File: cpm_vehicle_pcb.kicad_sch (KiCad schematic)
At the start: 77 parts, among them IC1 ATMEGAAU, IC2 RPI-ZERO, J1 Conn_02x03_Counter_Clockwise, J2 Conn_02x03_Counter_Clockwise, J3 Conn_01x05, J4 AVR-ISP-6, P1 NCP1117, P2 OSTTE020104, Q01 IRF3808, Q11 BSS123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

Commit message: BMS
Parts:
- added C8, C9: 100nF, footprints_vehicle_pcb:C0805_10681391, symbol main_board_V2.4-eagle-import:embedded_10681391_C-EUC0805
- added Q2, Q3: DMG9926UDM, Package_TO_SOT_SMD:SOT-23-6, symbol Transistor_FET:DMG9926UDM
- added R22, R24: 330, symbol Device:R
- added R23, R25: 2.7K, symbol Device:R
- added U5, U6: AP9101CK6, Package_TO_SOT_SMD:SOT-23-6, symbol Battery_Management:AP9101CK6
- C3: value 100nF -> 10uF
- C4, C7: value 100nF -> 22uF
- C5: value 100nF -> 10nuF
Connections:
- net GND: now also C3.2, C4.2, C5.2, C6.1, C7.1, MCP1.6 (VSS), R21.2, U4.2 (GND), C9.1, Q3.3 (S2), U6.6 (VSS)
- net +7.5V: now reaches C5.1, MCP1.7 (VBAT), SI1. (D)
- net +7.5V: now also R22.1
- new net: Q3.4 (G2), U6.1 (DO)
- new net: R25.1, U6.2 (VM)
- new net: Q3.6 (G1), U6.3 (CO)
- new net: C9.2, R24.2, U6.5 (VDD)
- new net: Q3.2 (S1/D2), Q3.5 (S1/D2)
- new net: Q2.2 (S1/D2), Q2.5 (S1/D2)
- new net: Q2.4 (G2), U5.1 (DO)
- new net: Q2.6 (G1), U5.3 (CO)
- new net: R23.1, U5.2 (VM)
- new net: C8.2, R22.2, U5.5 (VDD)
- new net +3.3V: C8.1, Q2.1 (D1), Q2.3 (S2), R23.2, R24.1, U5.6 (VSS)
- new net P-: Q3.1 (D1), R25.2
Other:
- note added: "Battery"
- note added: "Charger"

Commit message: usb to serial and some external pin and led circuit changes
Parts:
- added C10: 10nF, footprints_vehicle_pcb:C0805_10681391, symbol main_board_V2.4-eagle-import:embedded_10681391_C-EUC0805
- added J5: USB_B_Mini, symbol Connector:USB_B_Mini
- added QG2: XO91, footprints_vehicle_pcb:SM77H_crystal_oscillator, symbol main_board_V2.4-eagle-import:embedded_10681391_XO91
- added R26, R27: 1k, symbol Device:R
- added SW1: SW_DIP_x02, symbol Switch:SW_DIP_x02
- added U7: CH340G, Package_SO:SOIC-16_3.9x9.9mm_P1.27mm, symbol Interface_USB:CH340G
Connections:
- net +3V3: now also SW1.4; no longer C41.1, U3.1 (VCCA)
- net +5V: now also D2.2 (A), C10.2, J5.1 (VBUS), QG2.1 (E/D), QG2.4 (VCC), SW1.3, U7.16 (VCC); no longer C42.1, D2.1 (K), R10.2, U3.14 (VCCB)
- net ERW5: now also IC1.15 (PH3(OC4A)); no longer IC1.75 ((AD3)PA3)
- net ERW6: now also IC1.16 (PH4(OC4B)); no longer IC1.76 ((AD2)PA2)
- net ERW7: now also IC1.24 ((OC1A/PCINT5)PB5); no longer IC1.77 ((AD1)PA1)
- net ERW8: now also IC1.23 ((OC2A/PCINT4)PB4); no longer IC1.78 ((AD0)PA0)
- net GND: now also C10.1, J5.5 (GND), J5.6 (Shield), QG2.2 (GND), U7.1 (GND)
- net LED_BUILT_IN: now also IC1.25 ((OC1B/PCINT6)PB6), R10.2; no longer D3.2 (A), IC1.54 ((A9)PC1), R10.1
- net at R9.1: now also D2.1 (K); no longer D2.2 (A)
- net TX0: now reaches IC1.3 ((TXD0)PE1)
- net TX0: now also R27.2
- net RX0: now reaches IC1.4 ((XCK0/AIN0)PE2)
- net RX0: now also R26.2
- new net: D3.2 (A), R10.1
- new net: J5.2 (D-), U7.6 (UD-)
- new net: J5.3 (D+), U7.5 (UD+)
- new net: C42.1, SW1.2, U3.14 (VCCB)
- new net: C41.1, SW1.1, U3.1 (VCCA)
- new net: R27.1, U7.2 (TXD)
- new net: R26.1, U7.3 (RXD)
- new net: QG2.3 (OUT), U7.7 (XI)
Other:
- moved on the sheet: C71, D2, QG1, R10

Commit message: Small footprint changes
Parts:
- removed C01: 10uF, footprints_vehicle_pcb:UD-4X5,8_Electrolytic_cap, symbol main_board_V2.4-eagle-import:embedded_10681391_CPOL/4X5,8
- removed C02, C6, C8: 100nF, footprints_vehicle_pcb:C0805_10681391, symbol main_board_V2.4-eagle-import:embedded_10681391_C-EUC0805
- removed C5: 10nuF, footprints_vehicle_pcb:C0805_10681391, symbol main_board_V2.4-eagle-import:embedded_10681391_C-EUC0805
- removed D01: BAS40-04, footprints_vehicle_pcb:SOT23_BAS40_04_schottky_diode, symbol main_board_V2.4-eagle-import:embedded_10681391_BAS40-04
- removed D6: LED, symbol Device:LED
- removed MCP1: ~, symbol MCP73844:MCP73844
- removed Q01: IRF3808, footprints_vehicle_pcb:TO220_IRF3808PBF, symbol main_board_V2.4-eagle-import:embedded_10681391_IRF3808
- removed Q2: DMG9926UDM, Package_TO_SOT_SMD:SOT-23-6, symbol Transistor_FET:DMG9926UDM
- removed R03: 1.5k, footprints_vehicle_pcb:R0805_10681391, symbol main_board_V2.4-eagle-import:embedded_10681391_R-EUR0805
- removed R04: 12k, footprints_vehicle_pcb:R0805_10681391, symbol main_board_V2.4-eagle-import:embedded_10681391_R-EUR0805
- removed R05, R06: 0, footprints_vehicle_pcb:R0805_10681391, symbol main_board_V2.4-eagle-import:embedded_10681391_R-EUR0805
- removed R07, R08: 560k, footprints_vehicle_pcb:R0805_10681391, symbol main_board_V2.4-eagle-import:embedded_10681391_R-EUR0805
- removed R19: 100mΩ, PCM_JLCPCB:R_1206, symbol PCM_JLCPCB-Resistors:1206,100mΩ
- removed R20: R, symbol Device:R
- removed R22: 330, symbol Device:R
- removed R23: 2.7K, symbol Device:R
- removed Rk1, Rk2: 24k, footprints_vehicle_pcb:R0805_10681391, symbol main_board_V2.4-eagle-import:embedded_10681391_R-EUR0805
- removed SI1: ~, symbol SI9433:SI9433_MOSFET
- removed U1: LM385-1.2/NOPB, footprints_vehicle_pcb:SO08_LM385, symbol main_board_V2.4-eagle-import:embedded_10681391_LM385-1.2/NOPB
- removed U2: LM358D, footprints_vehicle_pcb:SO08_comparator, symbol main_board_V2.4-eagle-import:embedded_10681391_LM358D
- removed U5, U6: AP9101CK6, Package_TO_SOT_SMD:SOT-23-6, symbol Battery_Management:AP9101CK6
- added C11: 100nF, footprints_vehicle_pcb:C0805_10681391, symbol main_board_V2.4-eagle-import:embedded_10681391_C-EUC0805
- added R28: 330, Resistor_SMD:R_0603_1608Metric, symbol Device:R
- added SW2: SW_SPDT_312, Button_Switch_THT:SW_Slide-03_Wuerth-WS-SLTV_10x2.5x6.4_P2.54mm, symbol Switch:SW_SPDT_312
- added U8: R5460N, PCM_JLCPCB:SOT-23-6_L2.9-W1.6-P0.95-LS2.8-BL, symbol PCM_JLCPCB-Power:Battery, Li-Ion, 0.5A, TP4057
- C31: footprint footprints_vehicle_pcb:UD-6,3X5,8_Electrolytic_CAP -> Capacitor_SMD:C_1206_3216Metric
- C4, C7: value 22uF -> 220uF
- J5: footprint (none) -> Connector_USB:USB_Mini-B_AdamTech_MUSB-B5-S-VT-TSMT-1_SMD_Vertical
- R1, R10, R11, R12, R13, R14, R15, R16, R17, R18, R2, R3o1, R9: footprint footprints_vehicle_pcb:R0805_10681391 -> Resistor_SMD:R_0603_1608Metric
- R24: value 330 -> 1K; footprint (none) -> Resistor_SMD:R_0603_1608Metric
- R25: value 2.7K -> 330; footprint (none) -> Resistor_SMD:R_0603_1608Metric
- R26, R27: footprint (none) -> Resistor_SMD:R_0603_1608Metric
- RV1: footprint (none) -> Potentiometer_SMD:Potentiometer_Bourns_3214W_Vertical
- SW1: footprint (none) -> Button_Switch_SMD:SW_DIP_SPSTx02_Slide_9.78x7.26mm_W8.61mm_P2.54mm
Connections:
- net BAT_GND is gone; now on net GND_battery: C81.-, P2.2
- net +7.5V: now also C3.1, D5.1 (K), SW2.2 (C)
- net GND: now also Q3.1 (D1), R24.2; no longer C3.2, C4.2, C7.1, C9.1, Q3.3 (S2), R21.2, U4.2 (GND)
- net VCC_BAT: no longer C61.1, C81.+, J3.2 (Pin_2), P1.3 (VIN), P2.1
- net at Q3.4 (G2): now also U8.1 (DOUT)
- net vcc_bat: now reaches R25.1
- net vcc_bat: now also C61.1, C81.+, J3.2 (Pin_2), P1.3 (VIN), P2.1, SW2.3 (A)
- net at Q3.6 (G1): now also U8.2 (COUT)
- net GND_battery: now reaches C9.2
- net GND_battery: now also C3.2, C4.2, C7.1, Q3.3 (S2), R21.2, U4.2 (GND), C11.2, U8.6 (VSS); no longer R24.2
- net +3.3V: no longer names the net of R24.1
- net +3.3V: now also U8.3 (V-)
- net P-: no longer names the net of R25.2
- net P-: now also C11.1, U8.5 (VDD); no longer Q3.1 (D1)
- new net: C9.1, R28.2, U8.4 (VC)
- new net BB: R28.1
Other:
- note removed: "Battery"
- moved on the sheet: C10, C3, C4, C61, C62, C63, C7, C71, D2, D3, D4, D5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

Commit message: update
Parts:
- C31: footprint Capacitor_SMD:C_1206_3216Metric -> Capacitor_THT:CP_Radial_D6.3mm_P2.50mm
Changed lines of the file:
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@@
 			)
 		)
-		(property "Footprint" "Capacitor_SMD:C_1206_3216Metric"
+		(property "Footprint" "Capacitor_THT:CP_Radial_D6.3mm_P2.50mm"
 			(at 414.02 76.2 0)
 			(effects

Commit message: Net class defined
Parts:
- C4, C7: value 220uF -> 22uF
- L1: value L -> 20uH
- R21: value R -> 3.3K; footprint (none) -> Resistor_SMD:R_0603_1608Metric
- R51, R52: footprint footprints_vehicle_pcb:R0805_10681391 -> Resistor_SMD:R_0603_1608Metric
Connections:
- net VCC_BAT is gone; now on net vcc_bat: R51.2
- net +7.5V: now also C81.+, P2.1
- net SERVO_PWM: now also IC1.7 ((OC3C/INT5)PE5)
- net vcc_bat: no longer C81.+, P2.1
- net TCK: no longer names the net of IC1.93 ((ADC4/TCK)PF4)
- net TDI: no longer names the net of IC1.90 ((ADC7/TDI)PF7)
- net TDO: no longer names the net of IC1.91 ((ADC6/TDO)PF6)
- net TMS: no longer names the net of IC1.92 ((ADC5/TMS)PF5)
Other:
- moved on the sheet: R24

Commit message: some minute changes
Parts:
- removed C31: 220uF, Capacitor_THT:CP_Radial_D6.3mm_P2.50mm, symbol main_board_V2.4-eagle-import:embedded_10681391_CPOL/6,3X7,7
- removed C63, C81: 220uF, footprints_vehicle_pcb:UD-6,3X5,8_Electrolytic_CAP, symbol main_board_V2.4-eagle-import:embedded_10681391_CPOL/6,3X7,7
- removed D4, D5: D_Schottky, symbol Device:D_Schottky
- removed J4: AVR-ISP-6, footprints_vehicle_pcb:AVR_ISP_6_footprint, symbol Connector:AVR-ISP-6
- removed P2: OSTTE020104, TerminalBlock:TerminalBlock_MaiXu_MX126-5.0-02P_1x02_P5.00mm, symbol pole_screw_term_2:OSTTE020104
- added C31, C63: 220uF, footprints_vehicle_pcb:C0805_10681391, symbol main_board_V2.4-eagle-import:embedded_10681391_C-EUC0805
- added D1, D6: SS54, PCM_JLCPCB:D_SMA, symbol PCM_JLCPCB-Diodes:Schottky,SS54
- added J6: Conn_01x03_Socket, Connector_PinSocket_2.54mm:PinSocket_1x03_P2.54mm_Horizontal, symbol Connector:Conn_01x03_Socket
- C4, C7: footprint footprints_vehicle_pcb:C0805_10681391 -> Capacitor_SMD:C_0603_1608Metric
- J2: footprint footprints_vehicle_pcb:JST_B5B-XH-A -> footprints_vehicle_pcb:HARWIN_M20-9980346
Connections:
- net +5V: now also C31.1, C63.1
- net BB: now also J6.2 (Pin_2)
- net GND: now also C3.2, C4.2, C7.1, R21.2, U4.2 (GND), C31.2, C63.2
- net vcc_bat: now also SW2.2 (C); no longer R25.1, SW2.3 (A)
- net at C4.1, RV1.1: now also D1.1, D6.2
- net at L1.2, U4.1 (SW): now also D1.2
- net B+: now reaches SW2.1 (B)
- net B+: now also R25.1, J6.3 (Pin_3)
- net +7.5V renamed +8.5V
- net +8.5V: now also SW2.3 (A), D6.1; no longer SW2.2 (C)
- removed net GND_battery: C11.2, C3.2, C4.2, C7.1, C9.2, Q3.3 (S2), R21.2, U4.2 (GND), U8.6 (VSS)
- new net B-: C11.2, C9.2, J6.1 (Pin_1), Q3.3 (S2), U8.6 (VSS)
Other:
- note removed: "(For Powering ESC)"
- moved on the sheet: SW2

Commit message: update
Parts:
- added R3, R4: 10k, Resistor_SMD:R_0603_1608Metric, symbol Device:R
- L1: footprint (none) -> Inductor_SMD:L_10.4x10.4_H4.8
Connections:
- net +5V: now also R3.2, R4.2
- net SCL: now also R4.1
- net SDA: now also R3.1

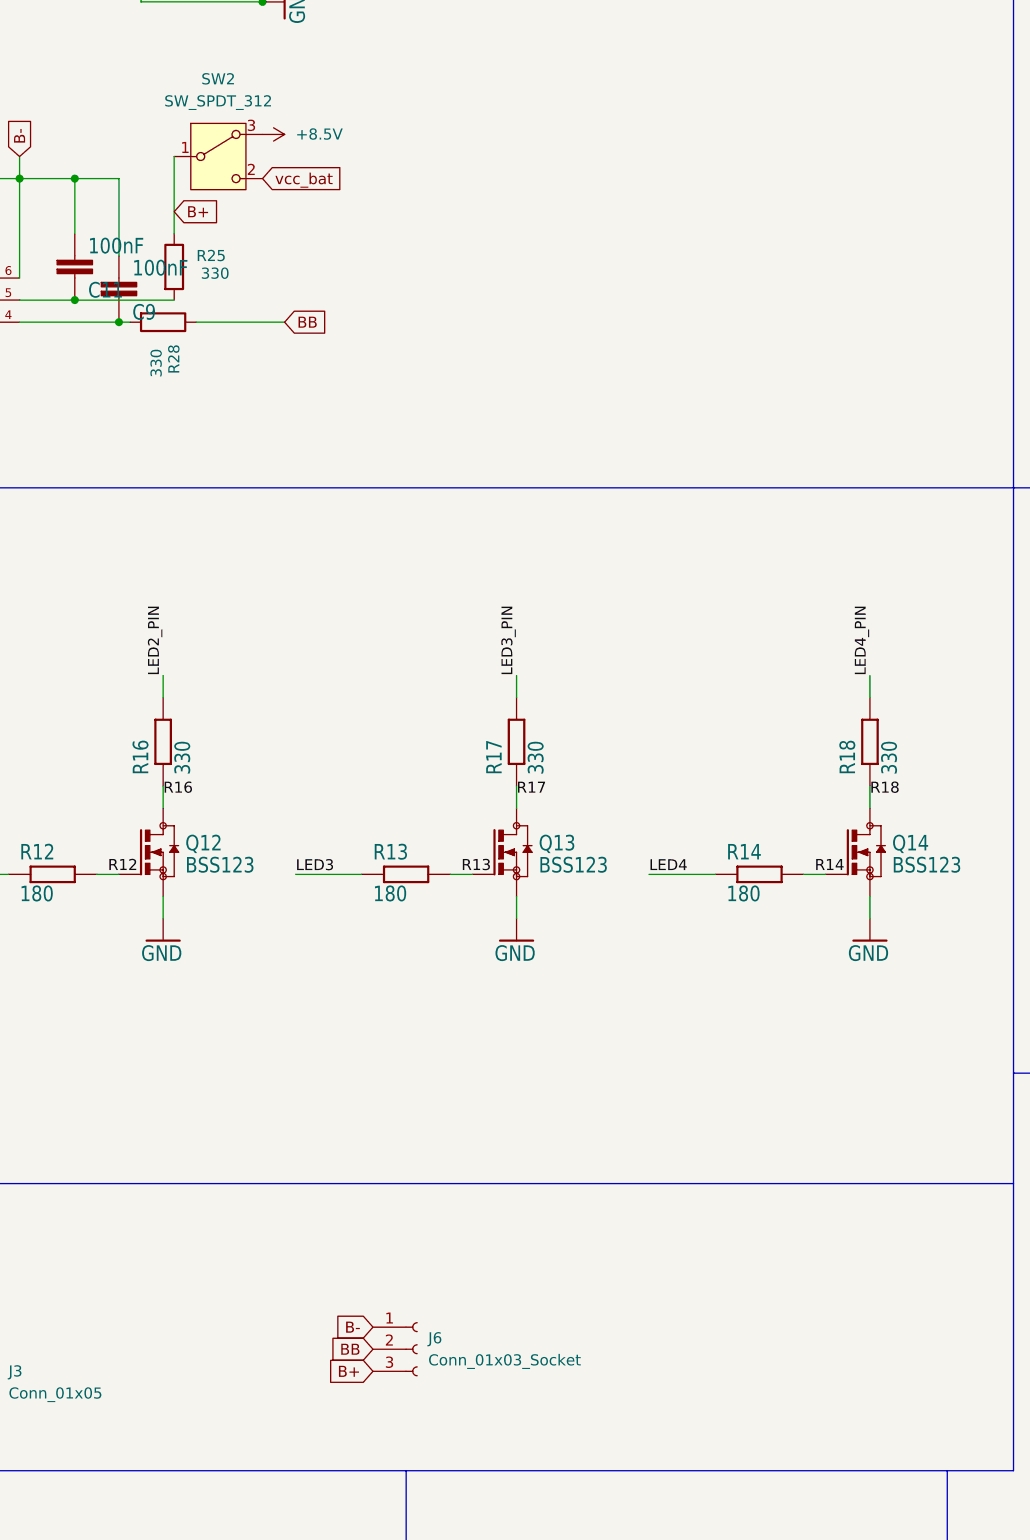
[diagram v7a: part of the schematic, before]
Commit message: Battery Protection Routing done
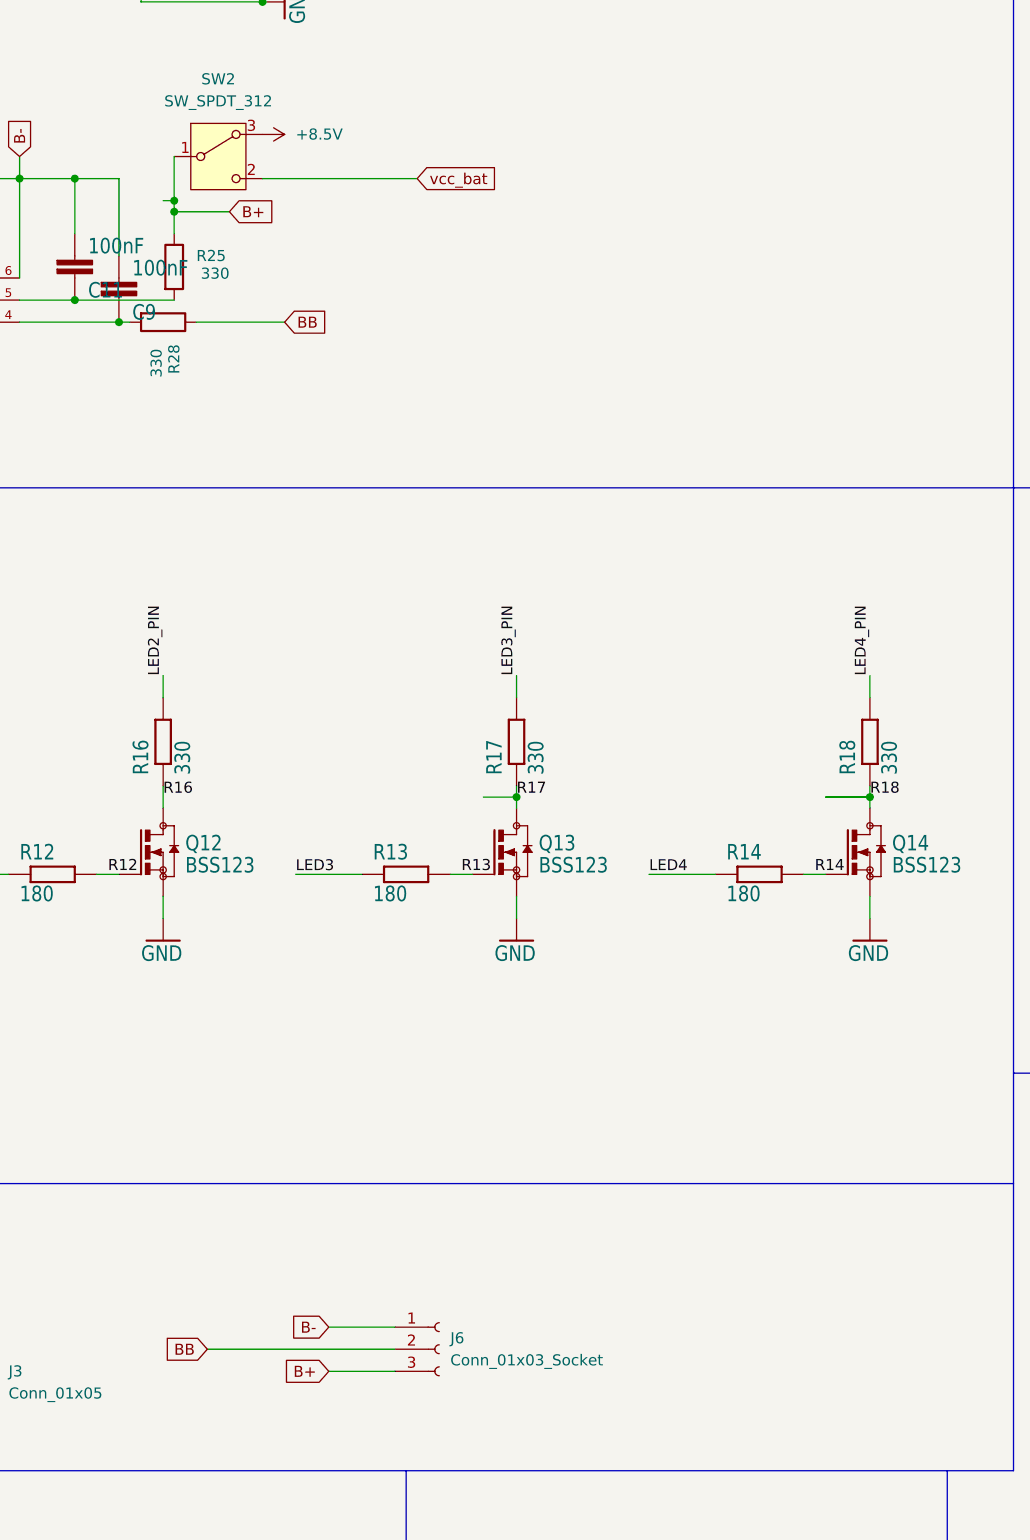
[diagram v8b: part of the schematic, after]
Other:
- moved on the sheet: J6
